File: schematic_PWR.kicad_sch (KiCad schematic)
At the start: 33 parts, among them J1 Conn_01x04, J14 STlink_v3, J2 Conn_01x04, J7 Conn_01x02, Q1 Q_PMOS_GSD, Q7 Q_PMOS_GSD, Q8 Q_PMOS_GSD, Q9 Q_PMOS_GSD, SW1 SW_SPST, SW3 SW_SPST, U1 MCP2562-H-SN

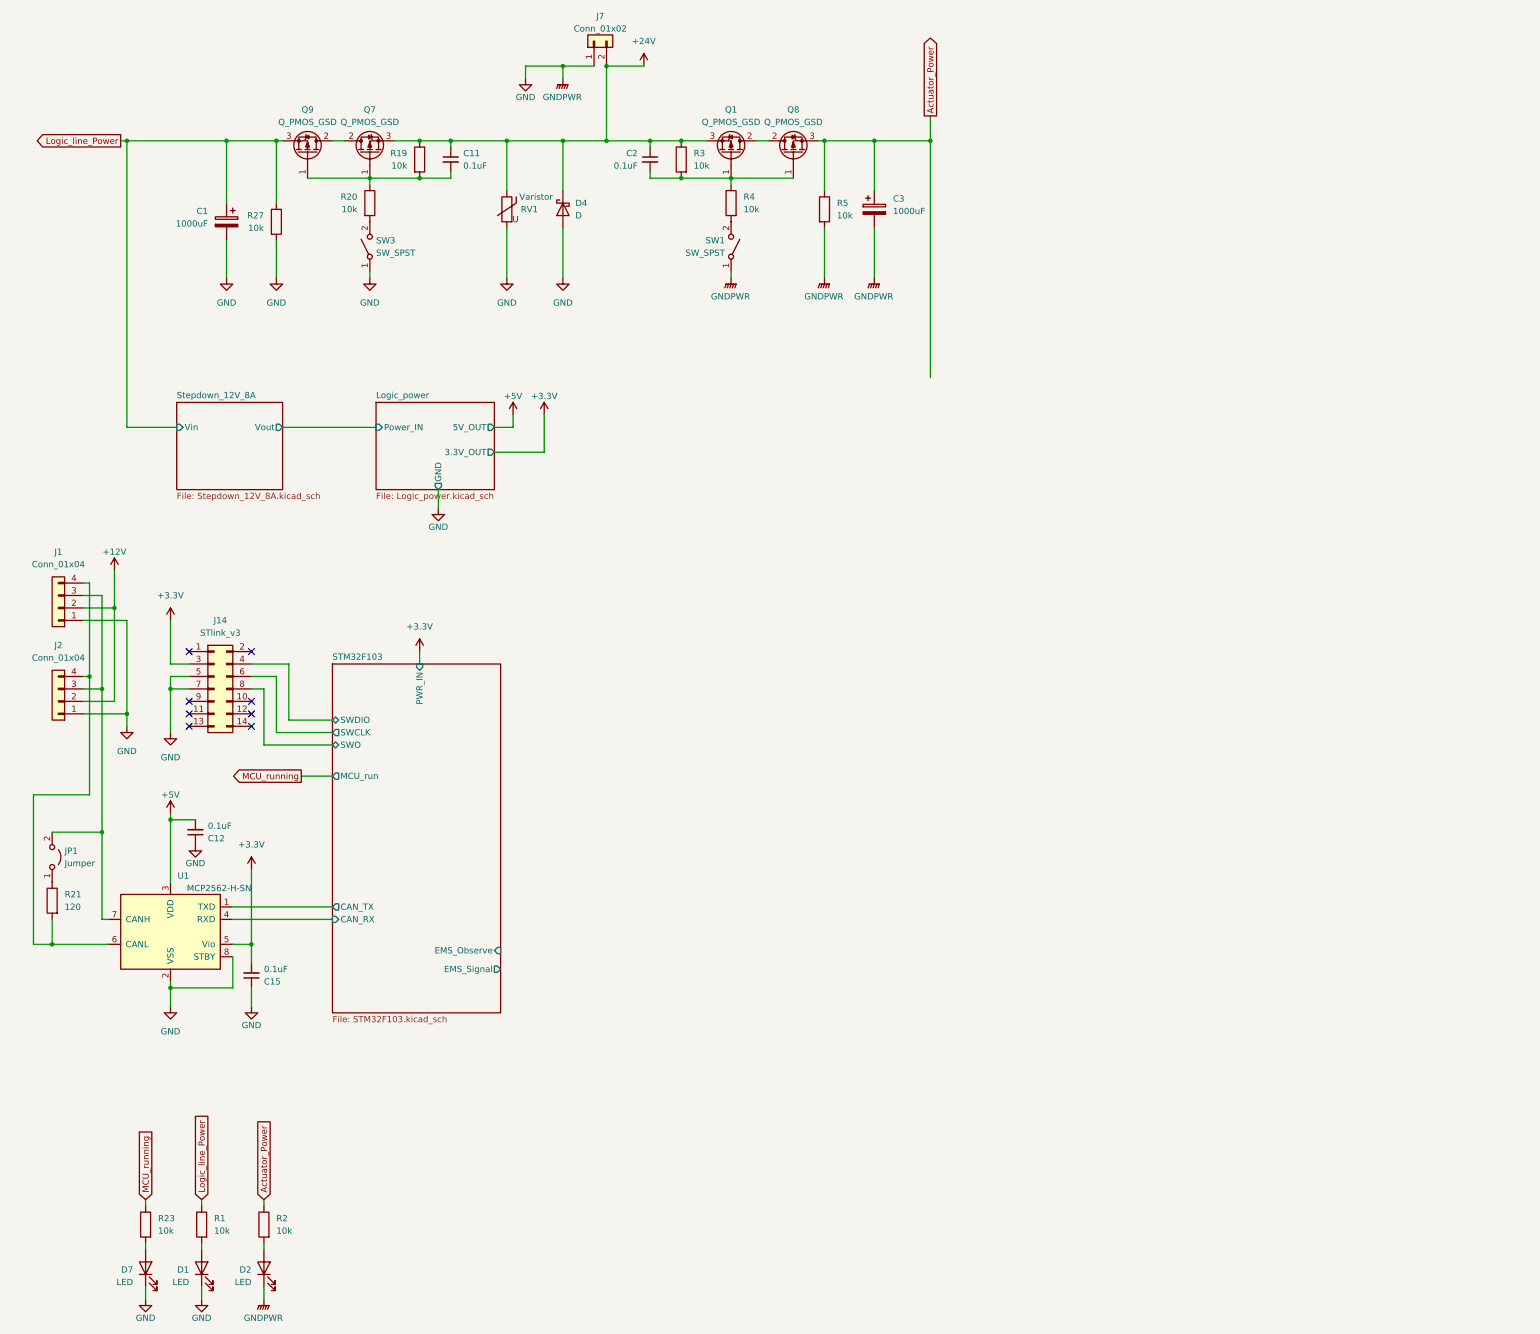
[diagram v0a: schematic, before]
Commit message: v0.2.0の回路を改良
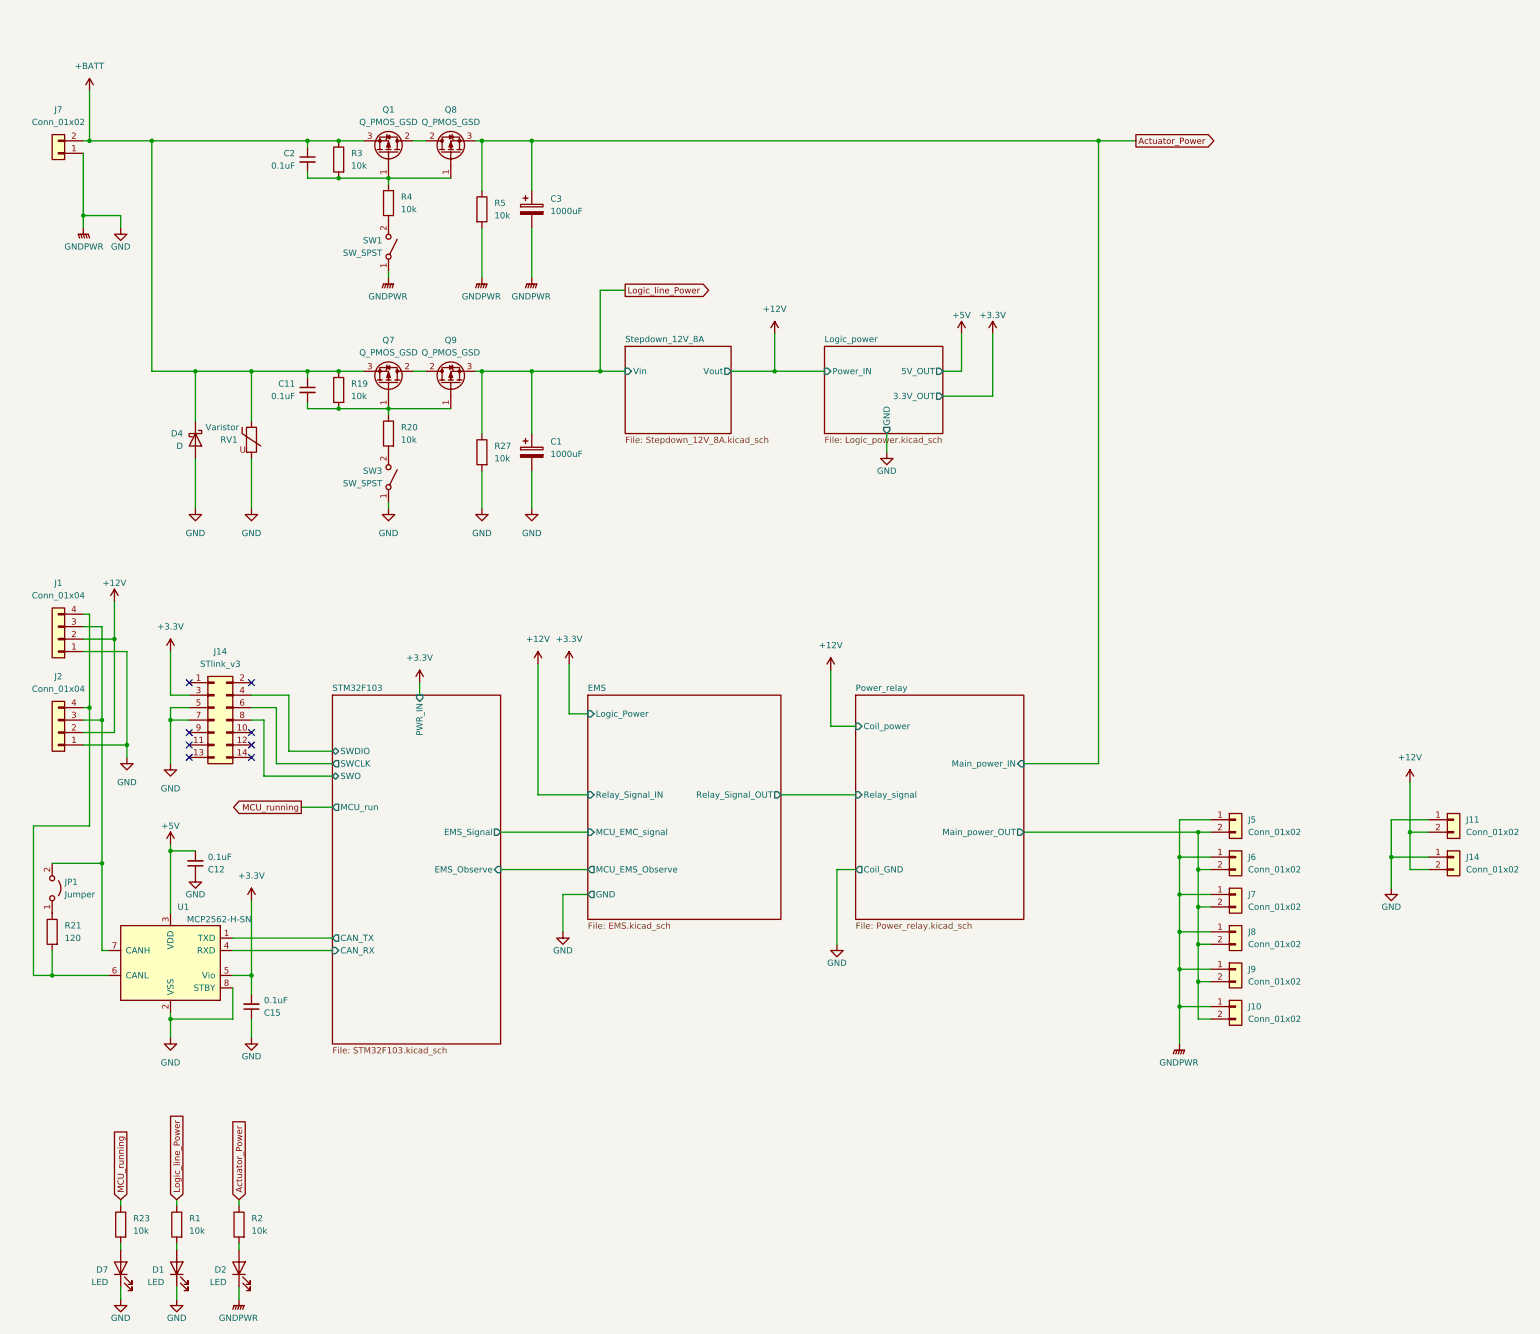
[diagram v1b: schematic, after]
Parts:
- added J10, J11, J14, J5, J6, J7, J8, J9: Conn_01x02, Connector_AMASS:AMASS_XT60-F_1x02_P7.20mm_Vertical, symbol Connector_Generic:Conn_01x02
- R5: footprint Resistor_THT:R_Axial_DIN0516_L15.5mm_D5.0mm_P20.32mm_Horizontal -> Resistor_THT:R_Axial_DIN0516_L15.5mm_D5.0mm_P5.08mm_Vertical
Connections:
- net +12V: now also J11.2 (Pin_2), J14.2 (Pin_2)
- net GND: now also J10.1 (Pin_1), J11.1 (Pin_1), J14.1 (Pin_1), J5.1 (Pin_1), J6.1 (Pin_1), J7.1 (Pin_1), J8.1 (Pin_1), J9.1 (Pin_1)
- net +24V renamed +BATT
- new net Power_relay/Main_power_OUT: J10.2 (Pin_2), J5.2 (Pin_2), J6.2 (Pin_2), J7.2 (Pin_2), J8.2 (Pin_2), J9.2 (Pin_2)
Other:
- added sheet EMS (EMS.kicad_sch)
- added sheet Power_relay (Power_relay.kicad_sch)
- moved on the sheet: C12, C15, C2, C3, D1, D2, D7, J1, J14, J2, J7, JP1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

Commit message: add footprint
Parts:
- added H1, H2, H3, H4: MountingHole, MountingHole:MountingHole_3.2mm_M3, symbol Mechanical:MountingHole
- J14: footprint RDC_general:JTAG_box_connector -> RDC_generic:JTAG_box_connector
- J7: footprint RDC_general:XT90-M -> RDC_generic:XT90-M
- SW1, SW3: footprint RDC_general:Toggle_switch -> RDC_generic:Toggle_switch
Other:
- sheet STM32F103 ports: added GND; removed none
- moved on the sheet: C1, J10, J5, J6, J7, J8, J9

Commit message: Parts layout finish
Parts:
- added C1: 100uF, Capacitor_THT:CP_Radial_D6.3mm_P2.50mm, symbol Device:C_Polarized
- added D2: LED, LED_SMD:LED_0603_1608Metric_Pad1.05x0.95mm_HandSolder, symbol Device:LED
- added R2: 10k, Resistor_SMD:R_0402_1005Metric, symbol Device:R
- C1: value 1000uF -> 100uF; footprint Capacitor_THT:CP_Radial_D16.0mm_P7.50mm -> Capacitor_THT:CP_Radial_D6.3mm_P2.50mm
- C11, C2: footprint Capacitor_SMD:C_0603_1608Metric_Pad1.08x0.95mm_HandSolder -> Capacitor_SMD:C_0603_1608Metric
- C12, C15: footprint Capacitor_SMD:C_0603_1608Metric_Pad1.08x0.95mm_HandSolder -> Capacitor_SMD:C_0402_1005Metric
- D4: footprint Diode_SMD:D_SOD-123 -> Diode_SMD:D_SOD-123F
- J1, J2: footprint Connector_JST:JST_XA_B04B-XASK-1_1x04_P2.50mm_Vertical -> Connector_JST:JST_XA_S04B-XASK-1_1x04_P2.50mm_Horizontal
- R1, R19, R2, R20, R23, R27, R3, R4: footprint Resistor_SMD:R_0603_1608Metric_Pad0.98x0.95mm_HandSolder -> Resistor_SMD:R_0402_1005Metric
- R21: footprint Resistor_SMD:R_0603_1608Metric_Pad0.98x0.95mm_HandSolder -> Resistor_SMD:R_0603_1608Metric
- renumbered H3 to H2, H2 to H3, J14 to J12
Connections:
- net +12V: now also C1.1
- net GND: now also C1.2, D2.1 (K)
- net Power_relay/Main_power_OUT: now also R2.1
- new net: D2.2 (A), R2.2
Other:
- moved on the sheet: C1, C11, C12, C15, C2, C3, D1, D2, D4, D7, J1, J10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

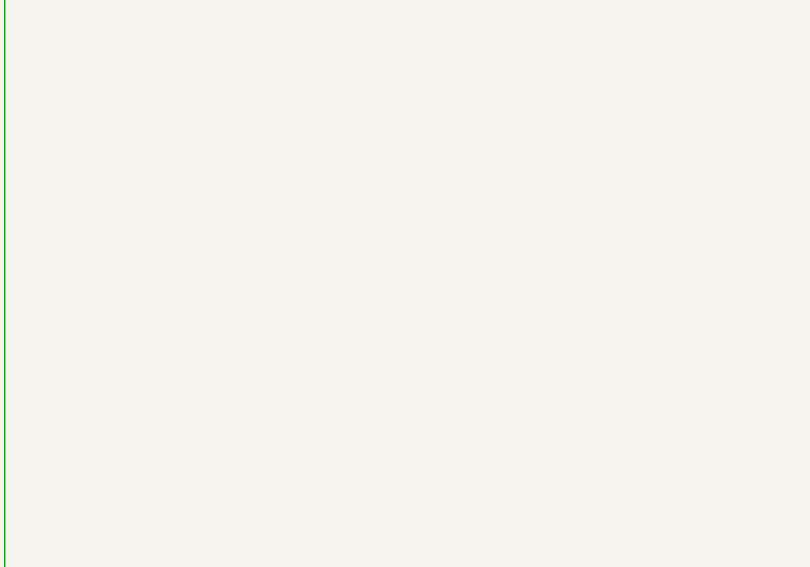
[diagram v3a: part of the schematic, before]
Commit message: add voltage detector
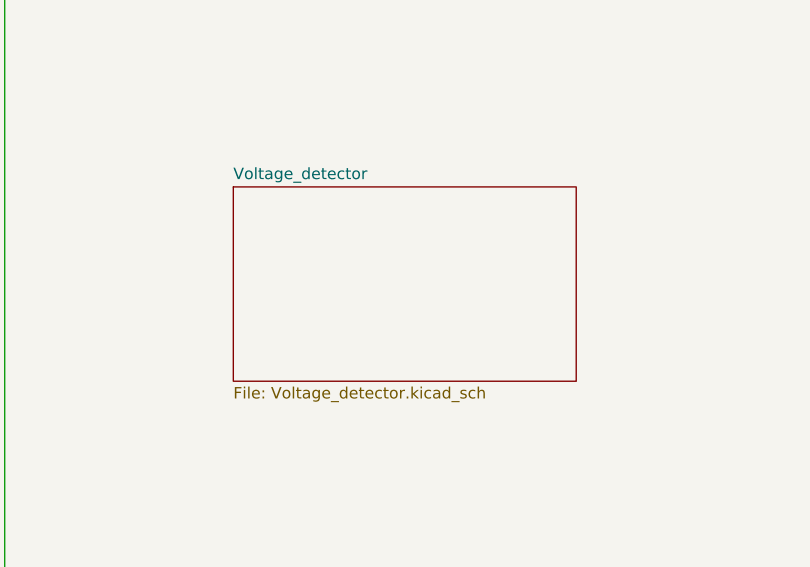
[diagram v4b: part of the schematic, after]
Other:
- added sheet Voltage_detector (Voltage_detector.kicad_sch)
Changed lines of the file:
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@@
+    )
+  )
+  (sheet (at 303.53 82.55) (size 38.1 21.59) (fields_autoplaced)
+    (stroke (width 0.1524) (type solid))
+    (fill (color 0 0 0 0.0000))
+    (property "Sheetname" "Voltage_detector" (at 303.53 81.8384 0)
+      (effects (font (size 1.27 1.27)) (justify left bottom))
+    )
+    (property "Sheetfile" "Voltage_detector.kicad_sch" (at 303.53 104.7246 0)
+      (effects (font (size 1.27 1.27)) (justify left top))
+    )
+    (instances
+      (project "schematic_PWR"
+        (path "/f4729e9b-1fa3-4d29-bc6f-94f153418360" (page "7"))
+      )
     )
   )

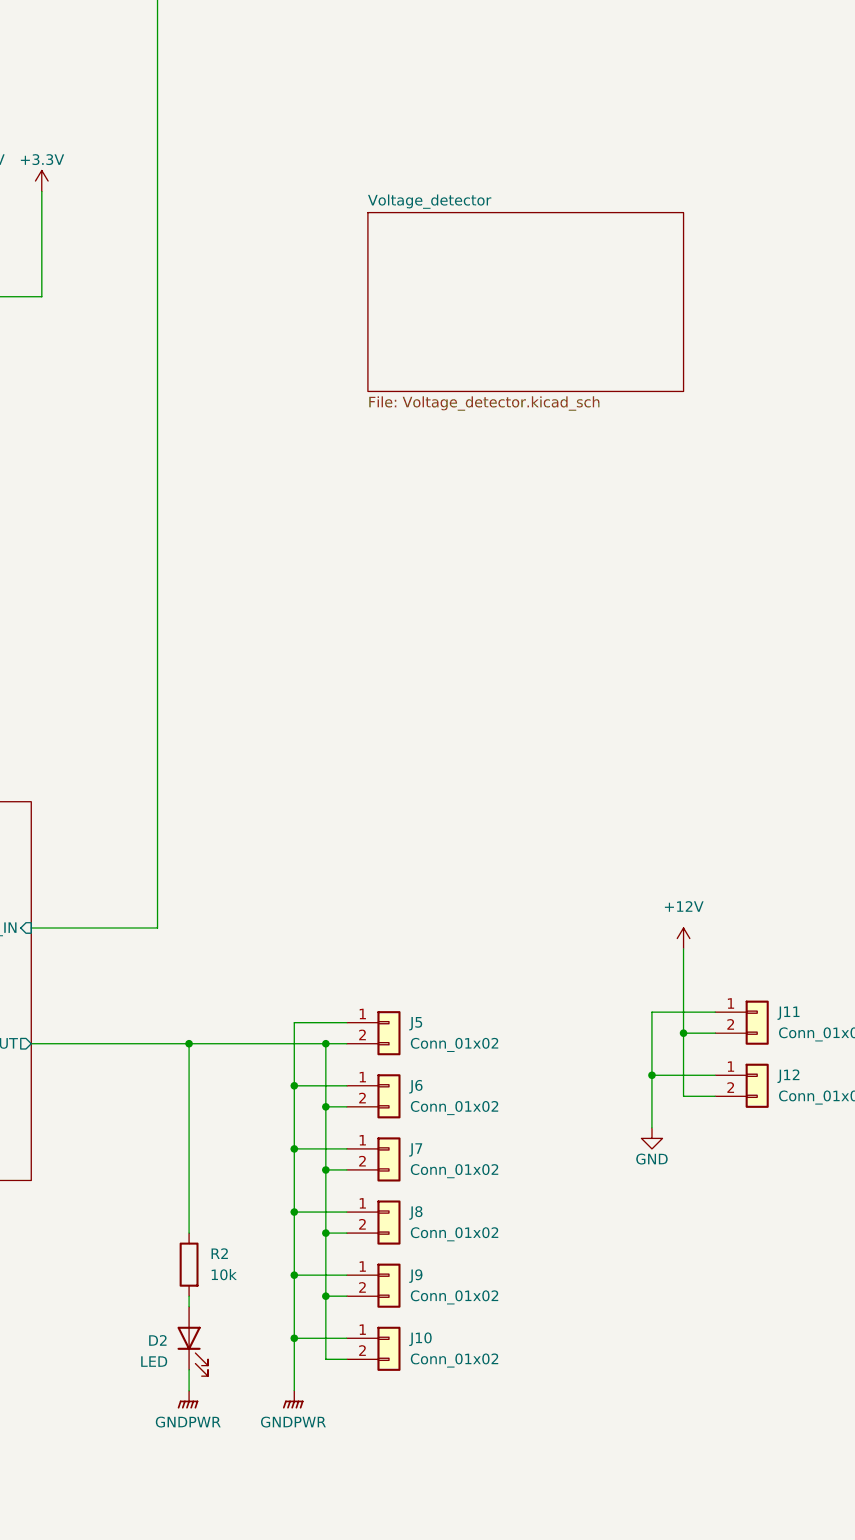
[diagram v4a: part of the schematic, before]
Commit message: update art work
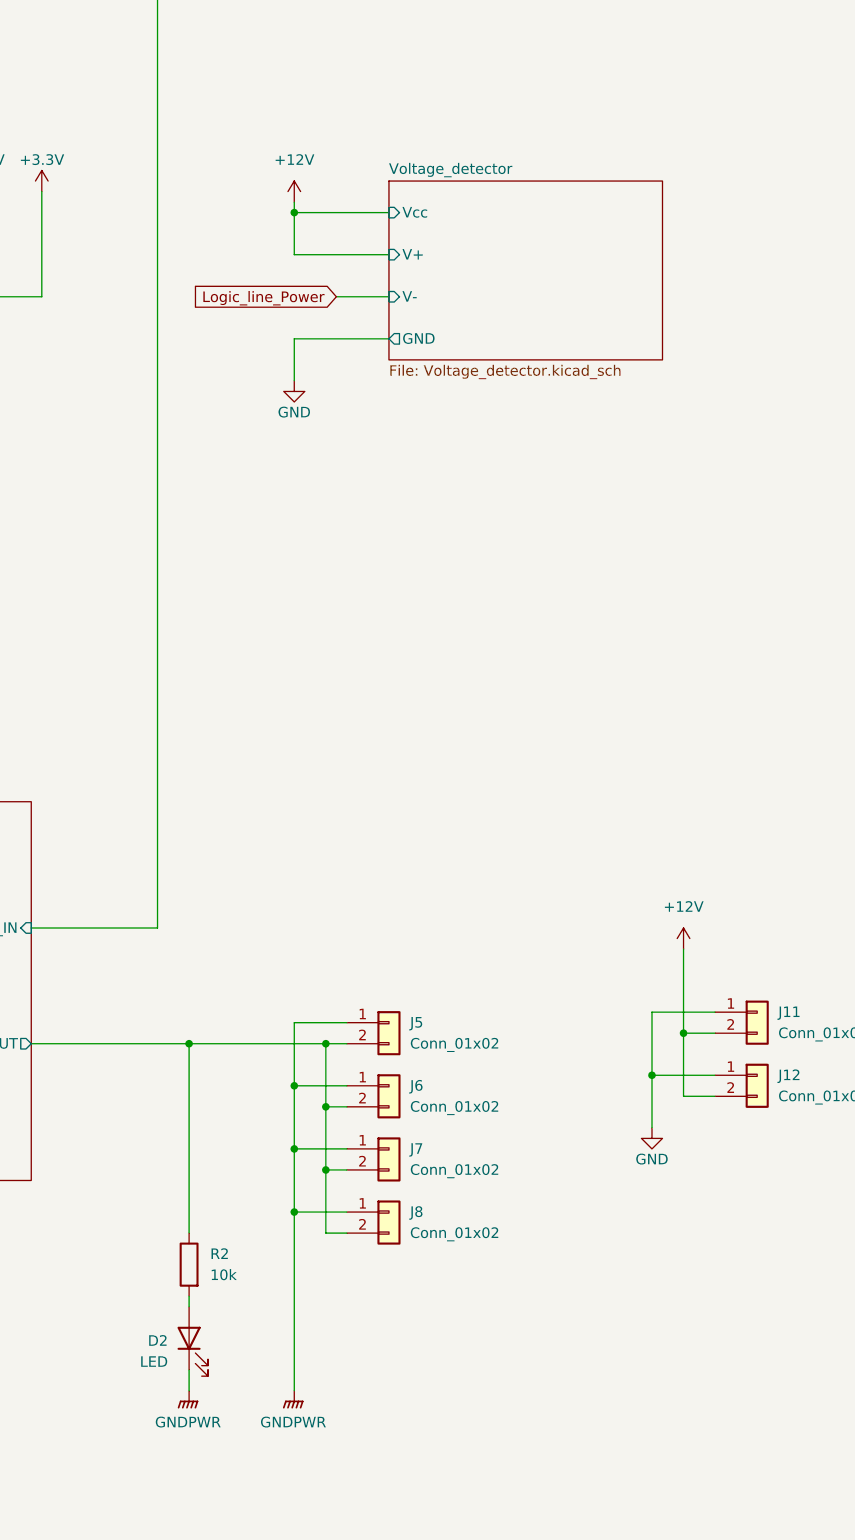
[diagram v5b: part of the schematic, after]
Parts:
- removed J10, J9: Conn_01x02, Connector_AMASS:AMASS_XT60-F_1x02_P7.20mm_Vertical, symbol Connector_Generic:Conn_01x02
- J11, J12: footprint Connector_AMASS:AMASS_XT60-F_1x02_P7.20mm_Vertical -> Connector_JST:JST_XA_S02B-XASK-1_1x02_P2.50mm_Horizontal
- J5, J6, J7, J8: footprint Connector_AMASS:AMASS_XT60-F_1x02_P7.20mm_Vertical -> Connector_AMASS:AMASS_XT60PW-F_1x02_P7.20mm_Horizontal
- R27: footprint Resistor_SMD:R_0402_1005Metric -> Resistor_SMD:R_1206_3216Metric
- R5: footprint Resistor_THT:R_Axial_DIN0516_L15.5mm_D5.0mm_P5.08mm_Vertical -> Resistor_SMD:R_1206_3216Metric
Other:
- sheet Voltage_detector ports: added GND, V+, V-, Vcc; removed none

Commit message: アートワークのほとんど終わり
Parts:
- removed C15: 0.1uF, Capacitor_SMD:C_0402_1005Metric, symbol Device:C_Small
- removed U1: MCP2562-H-SN, Package_SO:SOIC-8_3.9x4.9mm_P1.27mm, symbol Interface_CAN_LIN:MCP2562-H-SN
- added R27: 10k, Resistor_SMD:R_1206_3216Metric, symbol Device:R
- added U1: SN65HVD230, Package_SO:SOIC-8_3.9x4.9mm_P1.27mm, symbol Interface_CAN_LIN:SN65HVD230
- C1: name 50ZLH1000MEFC16X25 -> (none)
- C11, C2: LCSC (none) -> C14663
- C12: LCSC (none) -> C307331
- C3: name 16SEPF1000M -> (none)
- D1, D2: footprint LED_SMD:LED_0603_1608Metric_Pad1.05x0.95mm_HandSolder -> LED_SMD:LED_0603_1608Metric; LCSC (none) -> C2286
- D4: value D -> D_Schottky; LCSC (none) -> C22466353
- D7: footprint LED_SMD:LED_0603_1608Metric_Pad1.05x0.95mm_HandSolder -> LED_SMD:LED_0805_2012Metric; LCSC (none) -> C34499
- Q1, Q7, Q8, Q9: LCSC (none) -> C668678
- R1, R19, R2, R20, R3, R4: LCSC (none) -> C25744
- R21: LCSC (none) -> C22787
- R23: value 10k -> 1.2k; LCSC (none) -> C25862
- R27, R5: LCSC (none) -> C17902
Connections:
- net +12V: now also R27.1
- net +3.3V: now also C12.2, U1.3 (VCC)
- net +5V: no longer C12.2
- net GND: now also R27.2, U1.2 (GND), U1.8 (Rs)
- net STM32F103/CAN_RX: now also U1.4 (R)
- net STM32F103/CAN_TX: now also U1.1 (D)
- net at J1.3 (Pin_3), J2.3 (Pin_3), JP1.2 (B): now also U1.7 (CANH)
- net at J1.4 (Pin_4), J2.4 (Pin_4), R21.2: now also U1.6 (CANL)
- no-connect marks 8 -> 9
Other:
- sheet Stepdown_12V_8A ports: added GND; removed none
- moved on the sheet: C1
